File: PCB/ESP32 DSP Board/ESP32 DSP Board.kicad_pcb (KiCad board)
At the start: 4 copper layers, 92.5 x 59.5 mm, 89 parts, among them J1 USB4216-03-A_REVA, SW1 PTS810_SJM_250_SMTR_LFS, SW2 PTS810_SJM_250_SMTR_LFS, U8 ESP32-S3-WROOM-1, U9 TPS73733DCQ

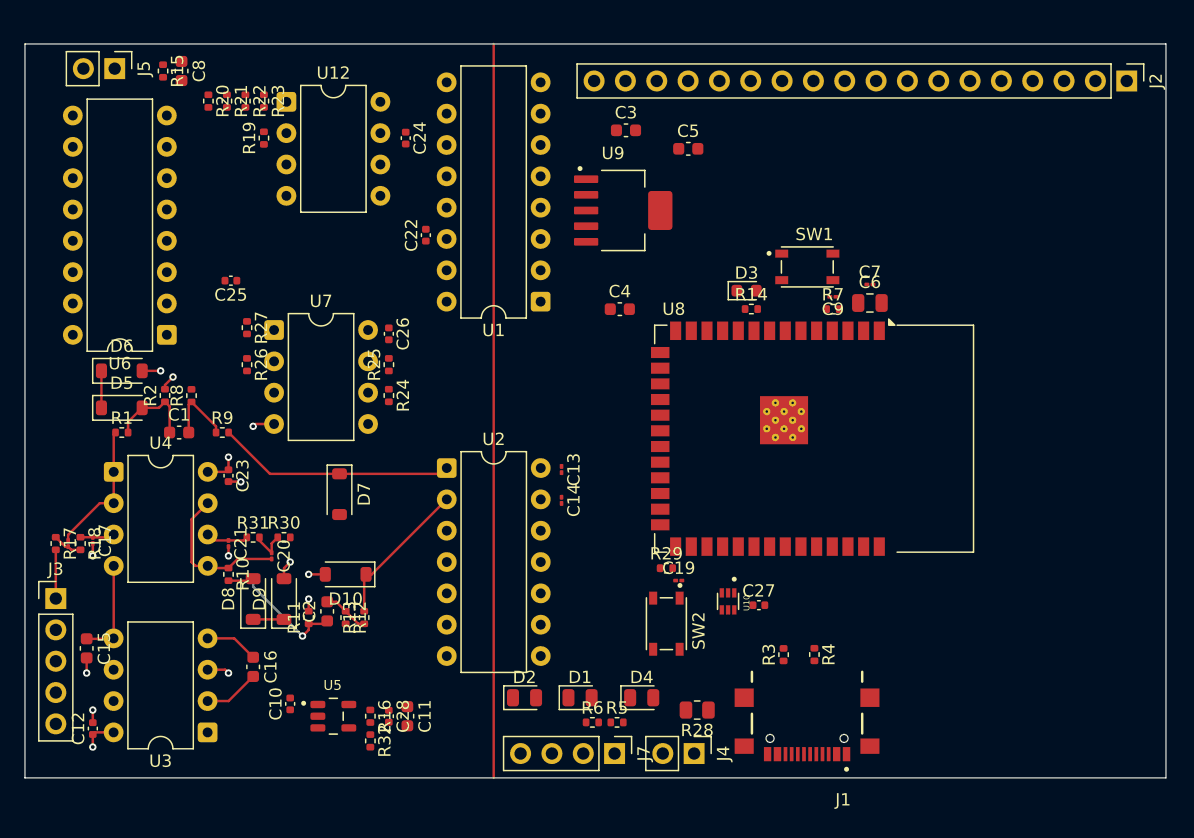
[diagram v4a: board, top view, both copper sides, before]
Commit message: Analog Side Routing Complete
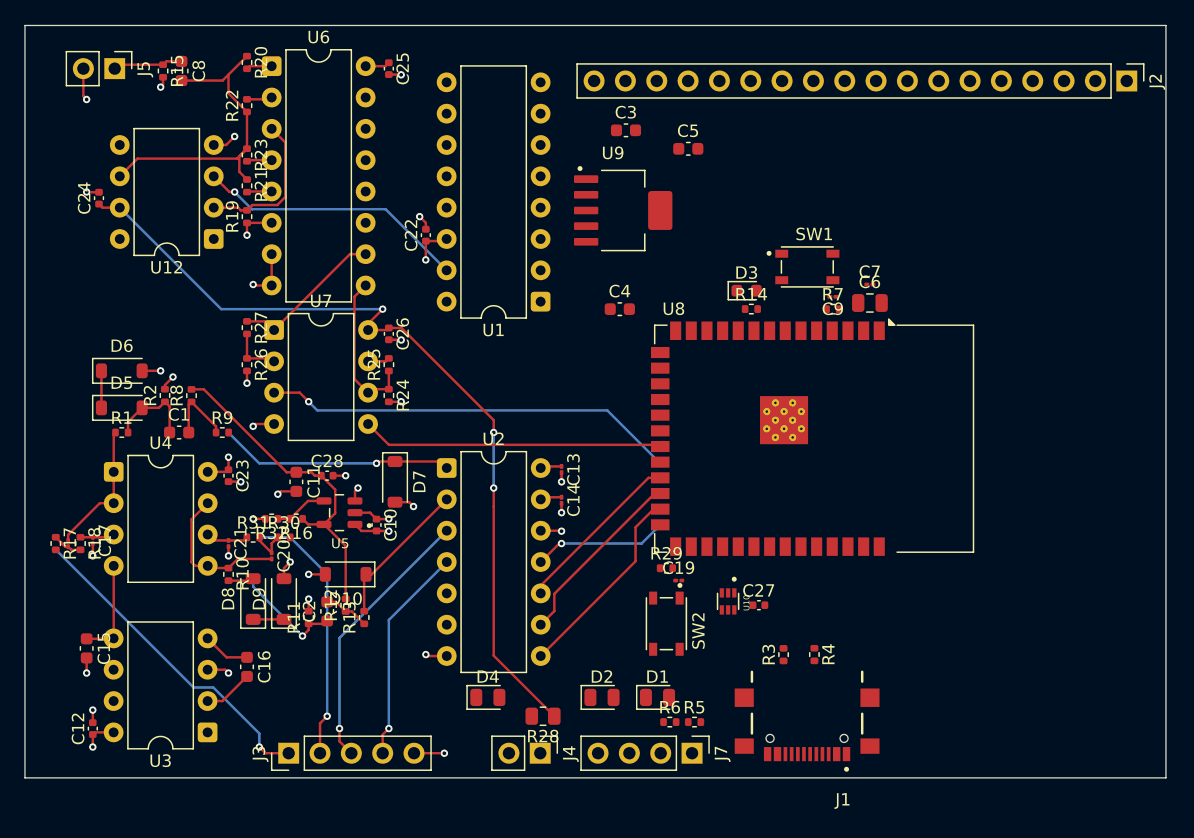
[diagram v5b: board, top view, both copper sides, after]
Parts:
- moved C24 25.3 mm to (92.5, 71.0), turned to 90 degrees
- moved U6 23.4 mm to (106.5, 60.3), turned to 0 degrees
- moved J3 22.7 mm to (107.9, 116.0), turned to 90 degrees
- moved C25 21.4 mm to (116.0, 60.5), turned to -90 degrees
- moved C11 21.0 mm to (108.5, 94.0)
- moved C28 20.1 mm to (111.0, 93.5), turned to 0 degrees
- moved R32 19.7 mm to (106.5, 97.0), turned to 180 degrees
- moved R16 17.1 mm to (108.5, 97.0), turned to 180 degrees
- moved U5 16.5 mm to (112.0, 96.5), turned to 180 degrees
- moved C10 16.1 mm to (115.0, 97.5), turned to -90 degrees
- moved U12 12.6 mm to (101.8, 74.3), turned to 180 degrees
- moved R28 12.5 mm to (128.5, 113.0)
- moved D4 12.5 mm to (124.0, 111.5)
- moved J4 12.5 mm to (128.3, 116.0)
- moved R21 7.06 mm to (104.5, 70.0)
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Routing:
- net VDD: track 0.00 -> 70.1 mm, vias 0 -> 3
- net GND: track 15.2 -> 49.6 mm, vias 12 -> 33
- net A: track 0.00 -> 33.7 mm, vias 0 -> 1
- net Net-(U12-OUT): track 0.00 -> 27.0 mm
- net 1.5V: track 0.00 -> 26.9 mm
- net B: track 0.00 -> 24.4 mm
- net ADC CH0: track 3.95 -> 26.4 mm, vias 0 -> 1
- net ADC CH2: track 0.00 -> 22.0 mm, vias 0 -> 1
- net DAC OUT: track 0.00 -> 22.0 mm, vias 0 -> 1
- net ADC CH1: track 0.00 -> 21.5 mm, vias 0 -> 1
- net ADC CH3: track 0.00 -> 17.7 mm, vias 0 -> 1
- net ADC CS: track 0.00 -> 16.2 mm
- net ADC Din: track 0.00 -> 14.9 mm
- net ADC Dout: track 0.00 -> 13.9 mm
- net 2B: track 0.00 -> 12.8 mm
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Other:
- board size 92.5 x 59.5 mm -> 92.5 x 61 mm

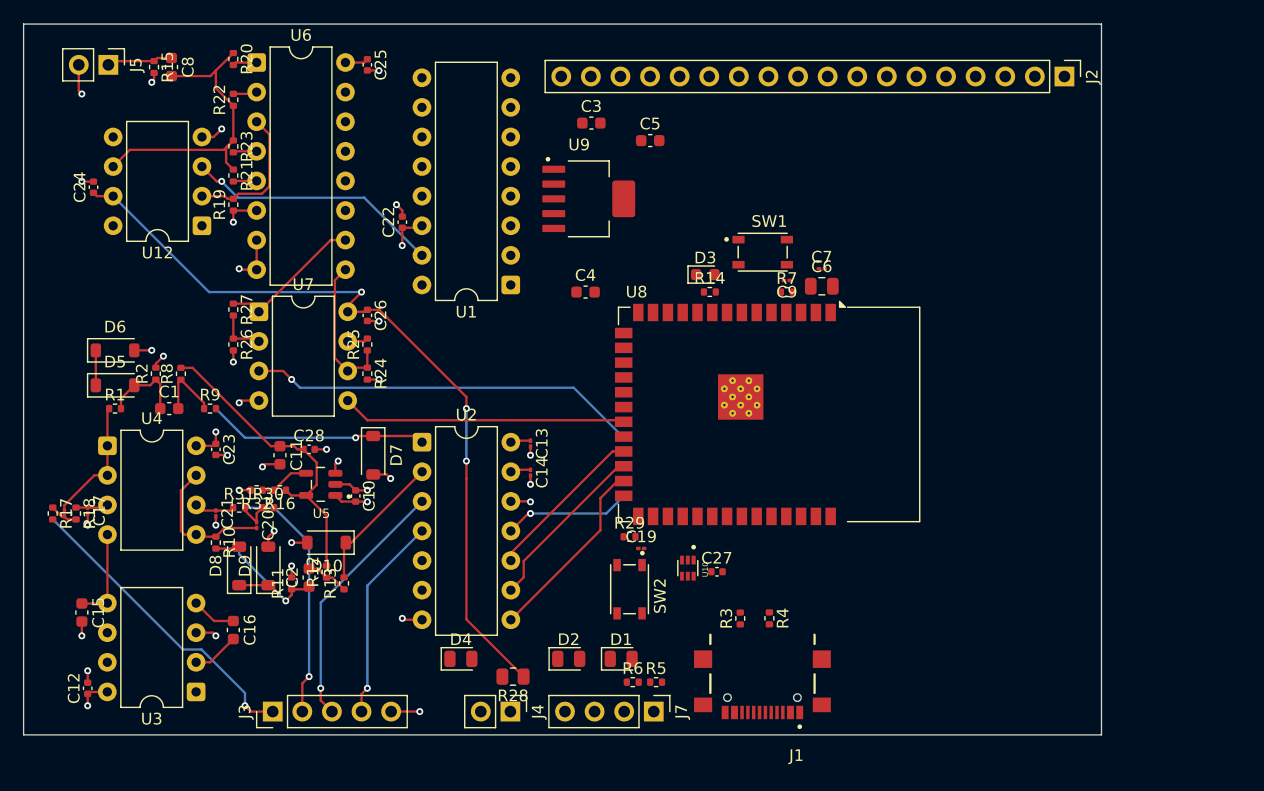
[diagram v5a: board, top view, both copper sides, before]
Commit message: Layer stackup changed to 6 layers, DAC routing started
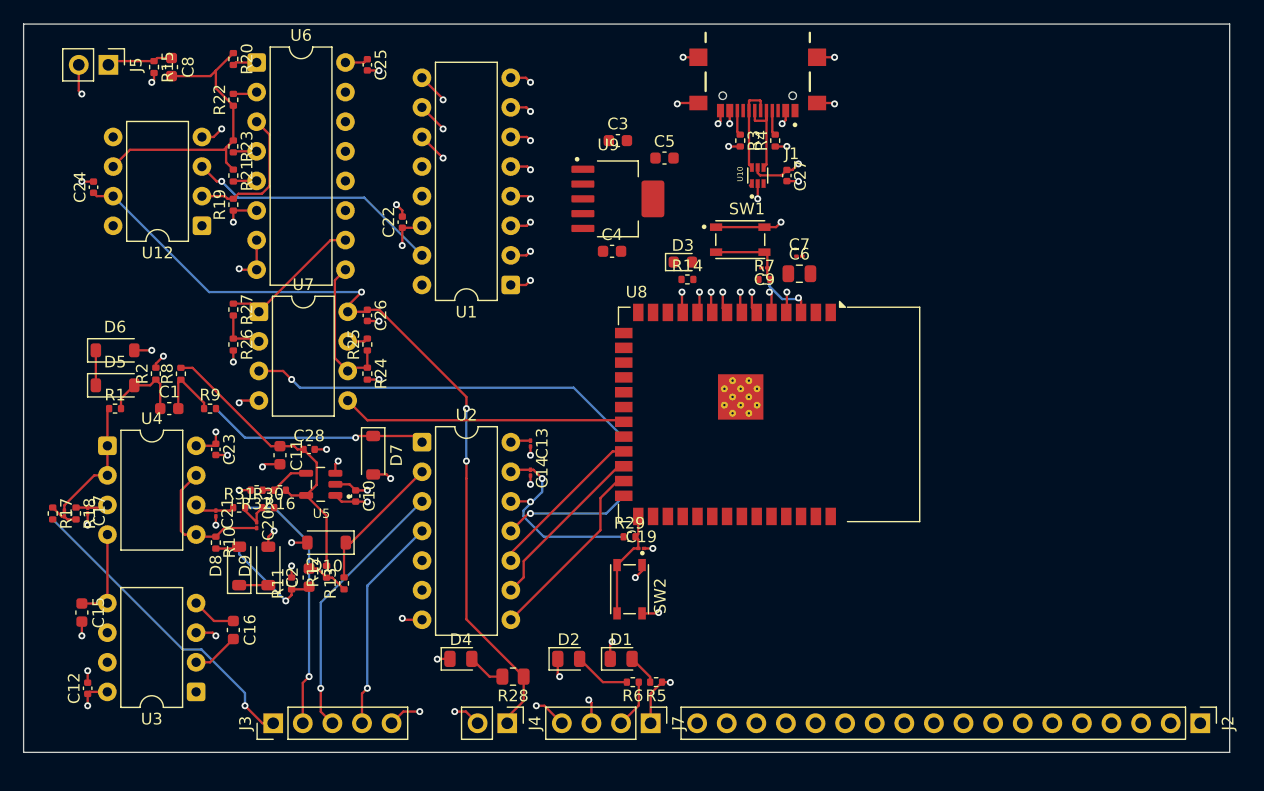
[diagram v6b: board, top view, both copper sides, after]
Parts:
- moved J2 56.7 mm to (187.5, 117.0)
- moved J1 51.7 mm to (149.5, 61.0)
- moved R3 41.0 mm to (148.0, 67.0), turned to -90 degrees
- moved R4 41.0 mm to (151.0, 67.0), turned to 90 degrees
- moved C27 34.5 mm to (152.0, 70.0), turned to -90 degrees
- moved U10 34.2 mm to (149.5, 70.0), turned to 90 degrees
- moved C4 4.17 mm to (137.0, 76.5)
- moved C3 2.73 mm to (137.5, 67.0)
- moved U9 2.50 mm to (137.5, 72.0)
- moved C6 2.20 mm to (153.1, 78.4)
- moved C7 2.20 mm to (153.1, 76.9)
- moved C9 2.20 mm to (150.1, 77.9)
- moved D3 2.20 mm to (143.1, 77.4)
- moved R7 2.20 mm to (150.1, 78.9)
- moved SW1 2.20 mm to (148.0, 75.5)
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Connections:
- J2 pad 1: IO4 -> GND
- J2 pad 10: IO3 -> IO38
- J2 pad 11: IO46 -> IO37
- J2 pad 12: IO9 -> IO36
- J2 pad 13: IO10 -> IO35
- J2 pad 14: IO11 -> IO12
- J2 pad 15: IO12 -> IO11
- J2 pad 16: GND -> IO10
- J2 pad 17: ESP Tx -> IO9
- J2 pad 18: ESP Rx -> +3V3
- J2 pad 2: IO5 -> IO1
- J2 pad 3: IO6 -> IO2
- J2 pad 4: IO7 -> ESP Tx
- J2 pad 5: IO15 -> ESP Rx
- J2 pad 6: IO16 -> IO42
- J2 pad 7: IO17 -> IO41
- J2 pad 8: IO18 -> IO40
- J2 pad 9: IO8 -> IO39
- R14 pad 2: Net-(U8-IO16) -> Net-(U8-IO8)
- U8 pad 10: IO17 -> DB1
- U8 pad 11: IO18 -> DB0
- U8 pad 12: IO8 -> Net-(U8-IO8)
- U8 pad 15: IO3 -> CS'
- U8 pad 16: IO46 -> WR'
- U8 pad 28: DB0 -> IO35
- U8 pad 29: DB1 -> IO36
- U8 pad 30: DB2 -> IO37
- U8 pad 31: DB3 -> IO38
- U8 pad 32: DB4 -> IO39
- U8 pad 33: DB5 -> IO40
- U8 pad 34: DB6 -> IO41
- U8 pad 35: DB7 -> IO42
- U8 pad 38: CS' -> IO2
- U8 pad 39: WR' -> IO1
- U8 pad 4: IO4 -> DB3
- U8 pad 5: IO5 -> DB4
- U8 pad 6: IO6 -> DB5
- U8 pad 7: IO7 -> DB6
- U8 pad 8: unconnected-(U8-IO15-Pad8) -> DB7
- U8 pad 9: Net-(U8-IO16) -> DB2
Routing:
- net GND: track 49.6 -> 88.0 mm, vias 33 -> 55
- net DB3: track 0.00 -> 34.5 mm, vias 0 -> 2
- net DB2: track 0.00 -> 34.3 mm, vias 0 -> 2
- net DB1: track 0.00 -> 32.2 mm, vias 0 -> 2
- net DB4: track 0.00 -> 30.6 mm, vias 0 -> 2
- net DB0: track 0.00 -> 29.6 mm, vias 0 -> 2
- net DB5: track 0.00 -> 28.1 mm, vias 0 -> 2
- net DB6: track 0.00 -> 26.0 mm, vias 0 -> 2
- net DB7: track 0.00 -> 23.5 mm, vias 0 -> 2
- net +3V3: track 1.76 -> 16.3 mm, vias 0 -> 1
- net Net-(U8-EN): track 0.00 -> 11.6 mm, vias 0 -> 1
- net +5V: track 14.7 -> 26.2 mm, vias 5 -> 9
- net BOOT: track 0.00 -> 9.51 mm
- net Net-(J1-DN1): track 0.00 -> 7.68 mm
- net Net-(J1-DP1): track 0.00 -> 7.68 mm
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- removed copper zone on In2.Cu, net +5V
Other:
- board size 92.5 x 61 mm -> 103.5 x 62.5 mm
- copper layers 4 -> 6

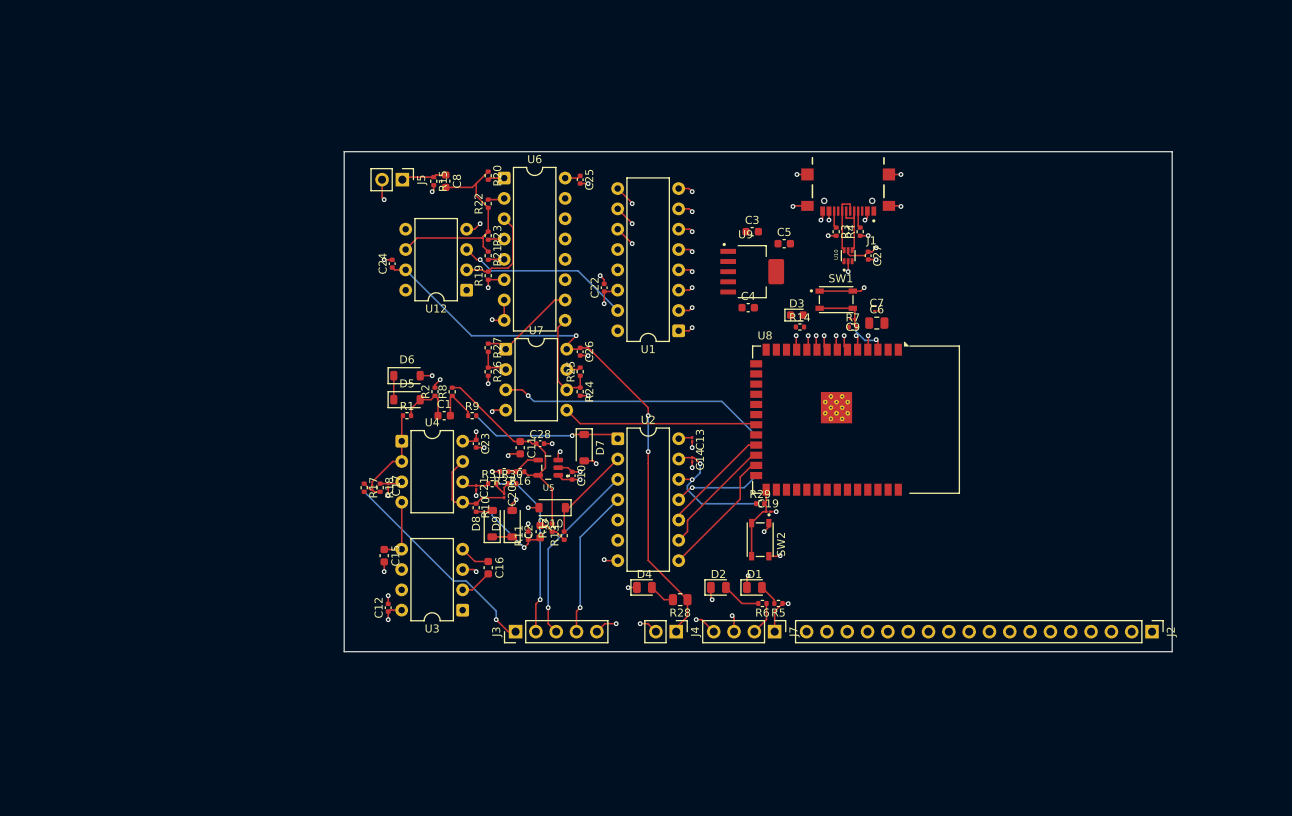
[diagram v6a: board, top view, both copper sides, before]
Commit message: Digital layout changed, pins moved closer to mcu, routing completed before checks
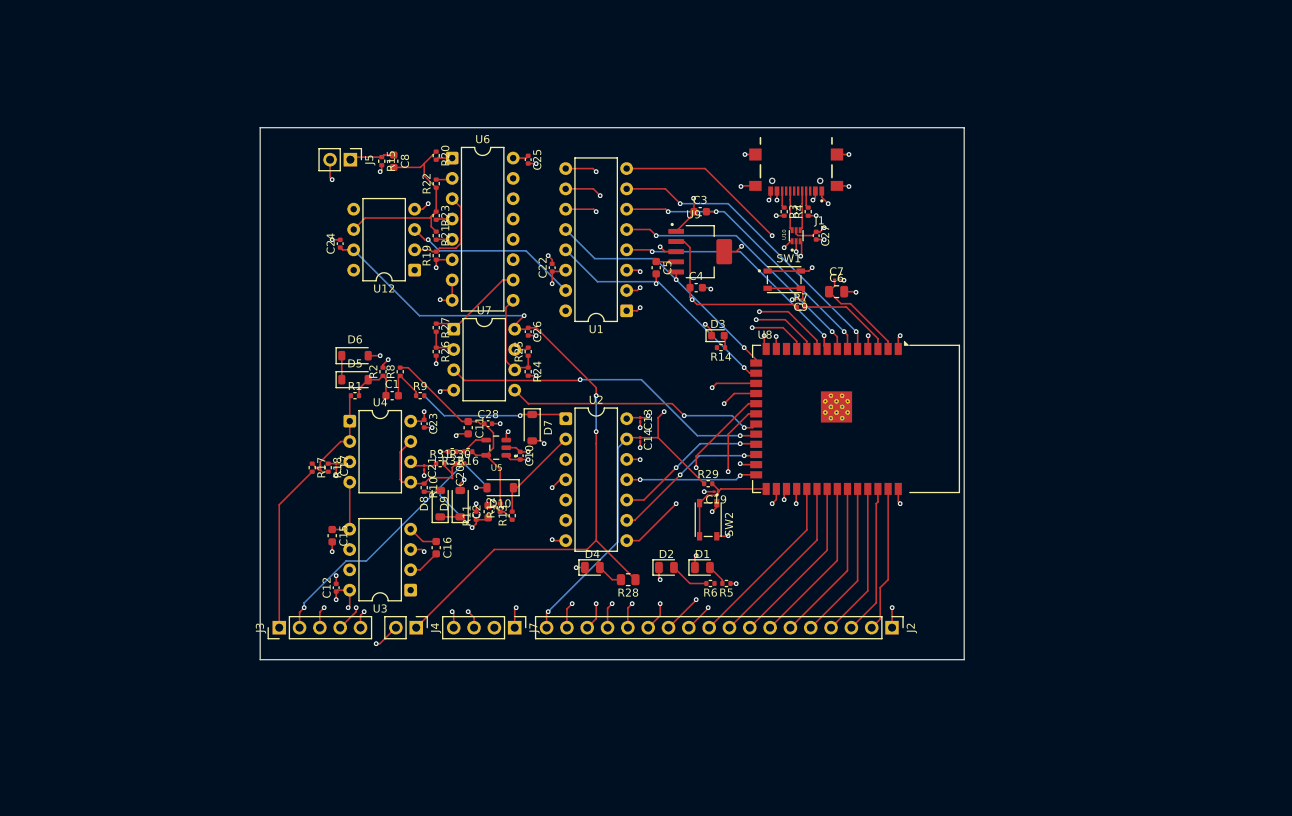
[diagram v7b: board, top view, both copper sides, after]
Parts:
- moved J2 32.5 mm to (155.0, 116.5)
- moved J4 32.5 mm to (95.5, 116.5)
- moved J7 32.5 mm to (107.8, 116.5)
- moved J3 29.5 mm to (78.4, 116.5)
- moved C5 16.3 mm to (125.5, 71.5), turned to -90 degrees
- moved R14 10.2 mm to (133.6, 81.5), turned to 180 degrees
- moved D3 10.2 mm to (133.2, 80.0)
- moved C1 6.96 mm to (92.5, 87.5)
- moved C10 6.96 mm to (108.5, 95.0)
- moved C11 6.96 mm to (102.0, 91.5)
- moved C12 6.96 mm to (85.5, 111.5)
- moved C13 6.96 mm to (123.5, 90.5)
- moved C14 6.96 mm to (123.5, 93.0)
- moved C15 6.96 mm to (85.0, 105.0)
- moved C16 6.96 mm to (98.0, 106.5)
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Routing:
- net +3V3: track 16.3 -> 93.7 mm, vias 1 -> 3
- net IO9: track 0.00 -> 43.6 mm, vias 0 -> 2
- net IO10: track 0.00 -> 39.6 mm, vias 0 -> 2
- net IO11: track 0.00 -> 36.3 mm, vias 0 -> 2
- net IO12: track 0.00 -> 33.9 mm, vias 0 -> 2
- net CS': track 0.35 -> 31.0 mm, vias 0 -> 1
- net WR': track 0.00 -> 30.2 mm, vias 0 -> 1
- net IO35: track 0.00 -> 24.9 mm, vias 0 -> 2
- net IO36: track 0.00 -> 23.5 mm, vias 0 -> 2
- net VDD: track 74.7 -> 97.6 mm
- net IO37: track 0.00 -> 22.9 mm, vias 0 -> 2
- net IO38: track 0.00 -> 22.4 mm
- net IO39: track 0.00 -> 21.9 mm
- net GND: track 88.0 -> 109.4 mm, vias 55 -> 68
- net IO40: track 0.00 -> 21.4 mm
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- added copper zone on In4.Cu, net +5V
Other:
- board size 103.5 x 62.5 mm -> 88 x 66.5 mm

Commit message: PCB finished pre-review
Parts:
- moved R7 4.52 mm to (148.0, 75.5), turned to 180 degrees
- moved U12 3.80 mm to (91.5, 71.8)
- moved C24 3.80 mm to (82.2, 68.5)
- moved C17 3.44 mm to (82.1, 96.8)
- moved C18 3.44 mm to (80.1, 97.0)
- moved C21 3.44 mm to (93.1, 97.0)
- moved C23 3.44 mm to (93.1, 91.5)
- moved R10 3.44 mm to (93.1, 99.5)
- moved R17 3.44 mm to (79.1, 97.0)
- moved R18 3.44 mm to (81.1, 97.0)
- moved U4 3.44 mm to (83.8, 91.2)
- moved C11 2.52 mm to (99.5, 91.2), turned to 180 degrees
- moved C16 2.44 mm to (99.0, 108.7)
- moved C6 2.19 mm to (150.0, 73.5)
- moved C7 2.19 mm to (150.0, 72.0)
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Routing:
- net +3.3V: track 0.00 -> 31.0 mm
- net VDD: track 97.6 -> 121.7 mm
- net Net-(U8-IO8): track 0.00 -> 9.96 mm
- net +3V3: track 93.7 -> 101.3 mm
- net ADC CH1: track 37.3 -> 30.6 mm, vias 1 -> 2
- net Net-(U12-In-): track 12.3 -> 16.1 mm
- net DAC OUT: track 22.0 -> 25.8 mm
- net Net-(D8-A): track 11.0 -> 14.8 mm, vias 1 -> 2
- net Net-(U4-2IN-): track 3.48 -> 6.58 mm
- net Net-(J1-DN1): track 4.99 -> 7.68 mm
- net Net-(J1-DP1): track 4.99 -> 7.64 mm
- net Net-(U3-C-): track 3.83 -> 6.47 mm
- net Net-(U12-OUT): track 27.0 -> 29.6 mm
- net CH0_FOUT: track 11.5 -> 13.6 mm
- net CH1_FOUT: track 12.3 -> 14.4 mm
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- added copper zone on In3.Cu, net GND
